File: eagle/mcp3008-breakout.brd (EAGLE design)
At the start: 17.4 x 22.9 mm, 4 parts

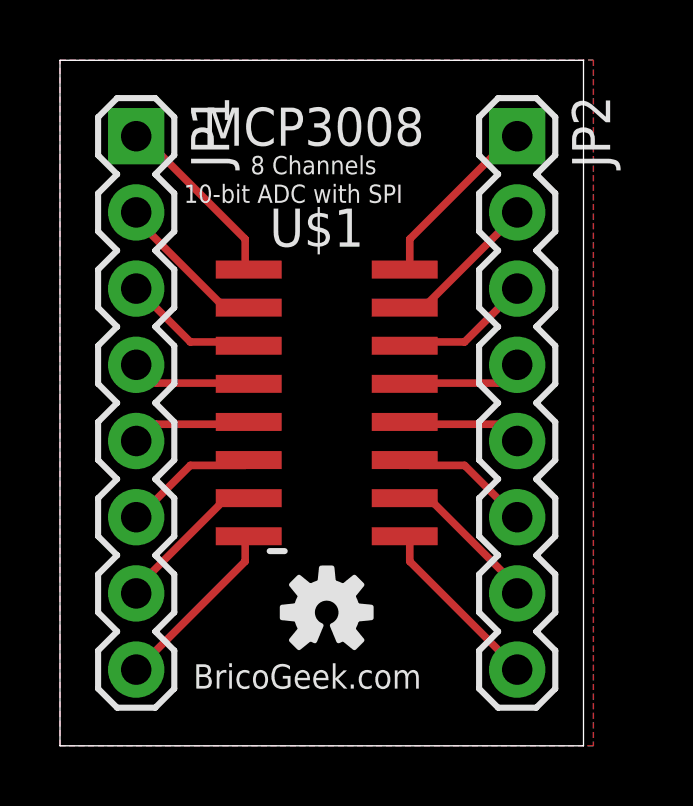
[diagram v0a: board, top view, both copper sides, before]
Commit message: Quitados los nombres de los componentes en tValues
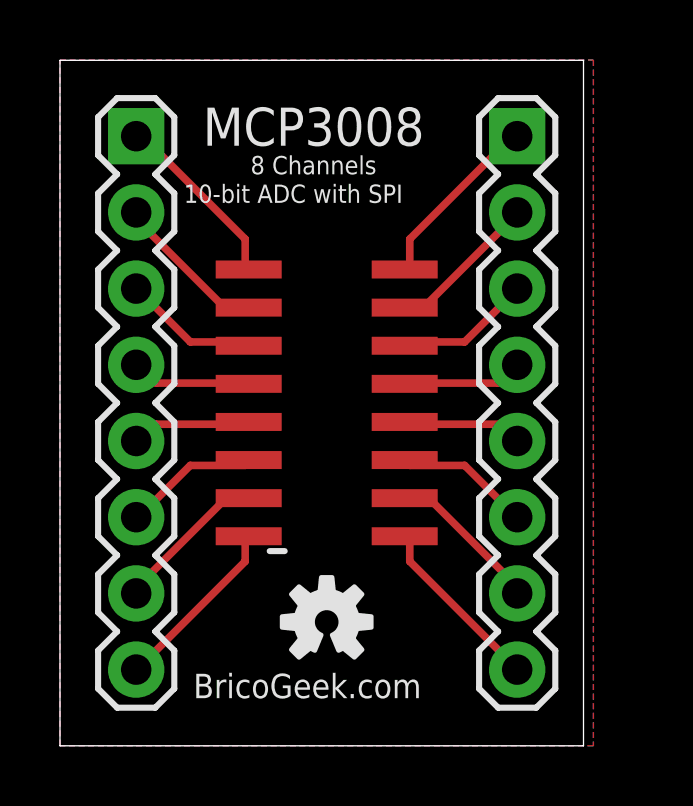
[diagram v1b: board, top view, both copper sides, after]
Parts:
- moved U$2 0.32 mm to (8.89, 4.13)
- renumbered U$1 to U1
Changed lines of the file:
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@@
 <layer number="21" name="tPlace" color="7" fill="1" visible="yes" active="yes"/>
 <layer number="22" name="bPlace" color="7" fill="1" visible="yes" active="yes"/>
-<layer number="23" name="tOrigins" color="15" fill="1" visible="no" active="yes"/>
+<layer number="23" name="tOrigins" color="15" fill="1" visible="yes" active="yes"/>
 <layer number="24" name="bOrigins" color="15" fill="1" visible="no" active="yes"/>
 <layer number="25" name="tNames" color="7" fill="1" visible="no" active="yes"/>
@@
 <text x="13.335" y="19.685" size="0.8128" layer="22" rot="MR0">VDD</text>
 <text x="10.16" y="17.4625" size="1.016" layer="22" rot="MR270">BricoGeek.com</text>
-<text x="4.445" y="1.905" size="0.8128" layer="21">BricoGeek.com</text>
+<text x="4.445" y="1.5875" size="0.8128" layer="21">BricoGeek.com</text>
 <text x="4.7625" y="20.0025" size="1.27" layer="21">MCP3008</text>
 <text x="6.35" y="19.05" size="0.6096" layer="21">8 Channels</text>
 <text x="4.1275" y="18.0975" size="0.6096" layer="21">10-bit ADC with SPI</text>
 <text x="8.5725" y="21.59" size="1.016" layer="22" rot="MR270">MCP3008 Breakout Board</text>
-<dimension x1="0" y1="22.86" x2="17.45" y2="22.85" x3="8.726459375" y3="25.40536875" textsize="1.016" layer="21"/>
-<dimension x1="0" y1="22.85" x2="0" y2="0" x3="-2.54" y3="11.425" textsize="1.016" layer="21"/>
 </plain>
 <attributes>
@@
 </autorouter>
 <elements>
-<element name="JP1" library="SparkFun-Connectors" package="1X08" value="" x="2.54" y="20.32" rot="R270"/>
-<element name="JP2" library="SparkFun-Connectors" package="1X08" value="" x="15.24" y="20.32" rot="R270"/>
-<element name="U$1" library="mcp3008-ok" package="SOIC16N" value="MCP3008" x="8.89" y="11.43" rot="R270"/>
-<element name="U$2" library="SparkFun-Aesthetics" package="OSHW-LOGO-S" value="" x="8.89" y="4.445"/>
+<element name="JP1" library="SparkFun-Connectors" package="1X08" value="" x="2.54" y="20.32" smashed="yes" rot="R270">
+<attribute name="VALUE" x="-0.635" y="21.59" size="1.27" layer="27" rot="R270"/>
+</element>
+<element name="JP2" library="SparkFun-Connectors" package="1X08" value="" x="15.24" y="20.32" smashed="yes" rot="R270">
+<attribute name="VALUE" x="12.065" y="21.59" size="1.27" layer="27" rot="R270"/>
+</element>
+<element name="U1" library="mcp3008-ok" package="SOIC16N" value="MCP3008" x="8.89" y="11.43" smashed="yes" rot="R270">
+<attribute name="VALUE" x="8.255" y="15.875" size="1.27" layer="27" rot="R270"/>
+</element>
+<element name="U$2" library="SparkFun-Aesthetics" package="OSHW-LOGO-S" value="" x="8.89" y="4.1275"/>
 </elements>
 <signals>
 <signal name="CH0">
 <contactref element="JP1" pad="1"/>
-<contactref element="U$1" pad="1"/>
+<contactref element="U1" pad="1"/>
 <wire x1="6.1722" y1="16.891" x2="6.1722" y2="15.9766" width="0.254" layer="1"/>
 <wire x1="2.7432" y1="20.32" x2="6.1722" y2="16.891" width="0.254" layer="1"/>
@@
 <signal name="CH1">
 <contactref element="JP1" pad="2"/>
-<contactref element="U$1" pad="2"/>
+<contactref element="U1" pad="2"/>
 <wire x1="5.4864" y1="14.605" x2="6.29" y2="14.605" width="0.254" layer="1"/>
 <wire x1="2.5146" y1="17.5768" x2="5.4864" y2="14.605" width="0.254" layer="1"/>
@@
 <signal name="CH2">
 <contactref element="JP1" pad="3"/>
-<contactref element="U$1" pad="3"/>
+<contactref element="U1" pad="3"/>
 <wire x1="4.3434" y1="13.462" x2="6.1722" y2="13.462" width="0.254" layer="1"/>
 <wire x1="2.7432" y1="15.0622" x2="4.3434" y2="13.462" width="0.254" layer="1"/>
@@
 <signal name="CH3">
 <contactref element="JP1" pad="4"/>
-<contactref element="U$1" pad="4"/>
+<contactref element="U1" pad="4"/>
 <wire x1="3.2004" y1="12.0904" x2="6.1722" y2="12.0904" width="0.254" layer="1"/>
 <wire x1="2.7432" y1="12.5476" x2="3.2004" y2="12.0904" width="0.254" layer="1"/>
@@
 <signal name="CH4">
 <contactref element="JP1" pad="5"/>
-<contactref element="U$1" pad="5"/>
+<contactref element="U1" pad="5"/>
 <wire x1="3.2004" y1="10.7188" x2="6.1722" y2="10.7188" width="0.254" layer="1"/>
 <wire x1="2.7432" y1="10.2616" x2="3.2004" y2="10.7188" width="0.254" layer="1"/>
@@
 <signal name="CH5">
 <contactref element="JP1" pad="6"/>
-<contactref element="U$1" pad="6"/>
+<contactref element="U1" pad="6"/>
 <wire x1="4.3434" y1="9.3472" x2="6.1722" y2="9.3472" width="0.254" layer="1"/>
 <wire x1="2.7432" y1="7.747" x2="4.3434" y2="9.3472" width="0.254" layer="1"/>
@@
 <signal name="CH6">
 <contactref element="JP1" pad="7"/>
-<contactref element="U$1" pad="7"/>
+<contactref element="U1" pad="7"/>
 <wire x1="5.4864" y1="8.2042" x2="6.1722" y2="8.2042" width="0.254" layer="1"/>
 <wire x1="2.5146" y1="5.2324" x2="5.4864" y2="8.2042" width="0.254" layer="1"/>
@@
 <signal name="CH7">
 <contactref element="JP1" pad="8"/>
-<contactref element="U$1" pad="8"/>
+<contactref element="U1" pad="8"/>
 <wire x1="6.1722" y1="6.1468" x2="6.1722" y2="6.8326" width="0.254" layer="1"/>
 <wire x1="2.7432" y1="2.7178" x2="6.1722" y2="6.1468" width="0.254" layer="1"/>
@@
 <signal name="VCC">
 <contactref element="JP2" pad="1"/>
-<contactref element="U$1" pad="16"/>
+<contactref element="U1" pad="16"/>
 <wire x1="11.6586" y1="16.891" x2="11.6586" y2="15.9766" width="0.254" layer="1"/>
 <wire x1="15.0876" y1="20.32" x2="11.6586" y2="16.891" width="0.254" layer="1"/>
@@
 <signal name="VREF">
 <contactref element="JP2" pad="2"/>
-<contactref element="U$1" pad="15"/>
+<contactref element="U1" pad="15"/>
 <wire x1="12.1158" y1="14.605" x2="11.49" y2="14.605" width="0.254" layer="1"/>
 <wire x1="15.0876" y1="17.5768" x2="12.1158" y2="14.605" width="0.254" layer="1"/>
@@
 <signal name="CLK">
 <contactref element="JP2" pad="4"/>
-<contactref element="U$1" pad="13"/>
+<contactref element="U1" pad="13"/>
 <wire x1="14.6304" y1="12.0904" x2="11.6586" y2="12.0904" width="0.254" layer="1"/>
 <wire x1="15.24" y1="12.7" x2="14.6304" y2="12.0904" width="0.254" layer="1"/>
@@
 <signal name="DOUT">
 <contactref element="JP2" pad="5"/>
-<contactref element="U$1" pad="12"/>
+<contactref element="U1" pad="12"/>
 <wire x1="14.6304" y1="10.7188" x2="11.6586" y2="10.7188" width="0.254" layer="1"/>
 <wire x1="15.0876" y1="10.2616" x2="14.6304" y2="10.7188" width="0.254" layer="1"/>
@@
 <signal name="DIN">
 <contactref element="JP2" pad="6"/>
-<contactref element="U$1" pad="11"/>
+<contactref element="U1" pad="11"/>
 <wire x1="13.4874" y1="9.3472" x2="11.6586" y2="9.3472" width="0.254" layer="1"/>
 <wire x1="15.0876" y1="7.747" x2="13.4874" y2="9.3472" width="0.254" layer="1"/>
@@
 <signal name="CS">
 <contactref element="JP2" pad="7"/>
-<contactref element="U$1" pad="10"/>
+<contactref element="U1" pad="10"/>
 <wire x1="12.3444" y1="8.2042" x2="11.6586" y2="8.2042" width="0.254" layer="1"/>
 <wire x1="15.3162" y1="5.2324" x2="12.3444" y2="8.2042" width="0.254" layer="1"/>
@@
 <signal name="GND">
 <contactref element="JP2" pad="8"/>
-<contactref element="U$1" pad="9"/>
+<contactref element="U1" pad="9"/>
 <wire x1="11.6586" y1="6.1468" x2="11.6586" y2="6.8326" width="0.254" layer="1"/>
 <wire x1="15.0876" y1="2.7178" x2="11.6586" y2="6.1468" width="0.254" layer="1"/>
@@
 <wire x1="15.0876" y1="2.7178" x2="15.24" y2="2.54" width="0.254" layer="1"/>
 <contactref element="JP2" pad="3"/>
-<contactref element="U$1" pad="14"/>
+<contactref element="U1" pad="14"/>
 <wire x1="13.4874" y1="13.462" x2="11.6586" y2="13.462" width="0.254" layer="1"/>
 <wire x1="15.0876" y1="15.0622" x2="13.4874" y2="13.462" width="0.254" layer="1"/>
